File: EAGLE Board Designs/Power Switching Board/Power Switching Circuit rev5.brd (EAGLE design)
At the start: 100.3 x 86.1 mm, 69 parts, among them J1 CONNECTOR-4_SOURIAU_, J2 CONNECTOR-3_8STA20435PN, J3 CONNECTOR-4_SOURIAU_, K1 RELAY_SOLIDSTATE_NO_CMX60D20, Q1 TRANSISTOR_N_MOS_2-7K1S_TK100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, Q2 TRANSISTOR_N_MOS_2-7K1S_TK100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, Q3 TRANSISTOR_N_MOS_2-7K1S_TK100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, Q4 TRANSISTOR_N_MOS_2-7K1S_TK100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, U1 LTC4421

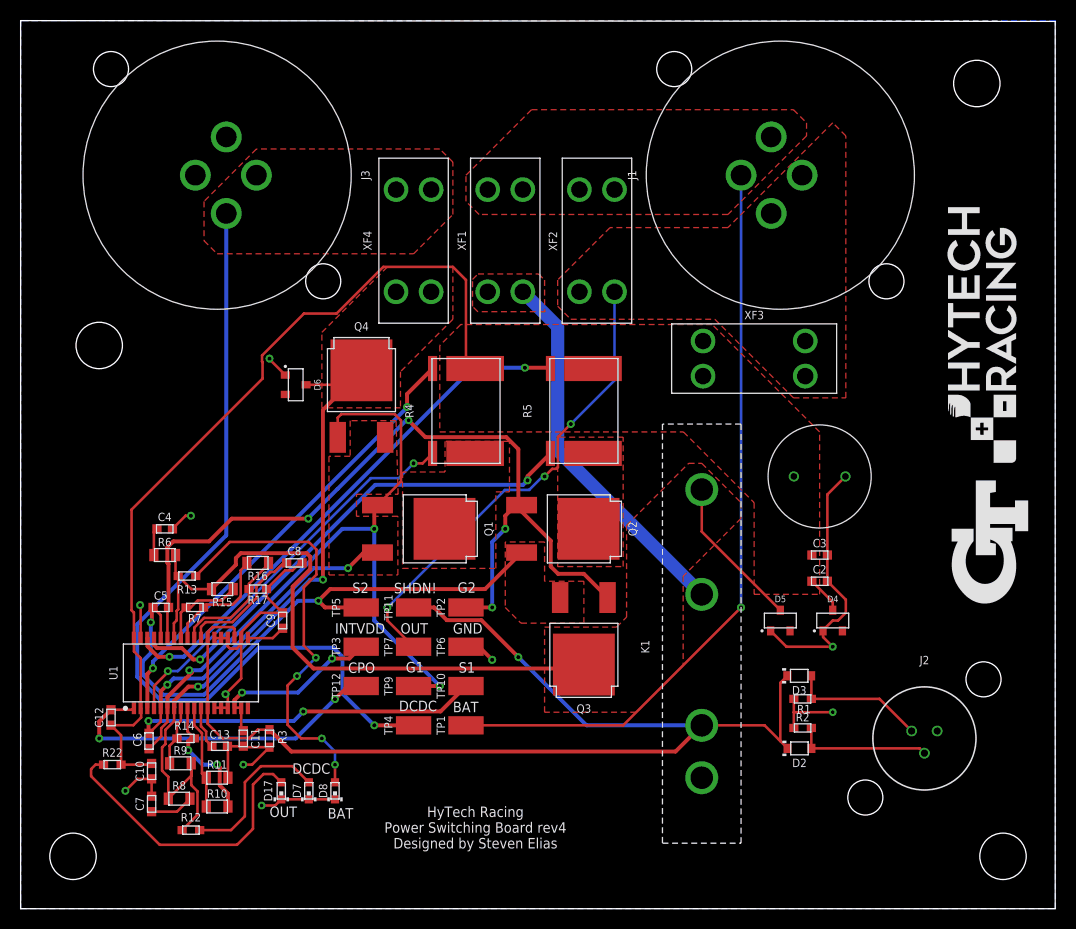
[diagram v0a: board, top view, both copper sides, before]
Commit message: Fixed issues with order of inputs to SSR
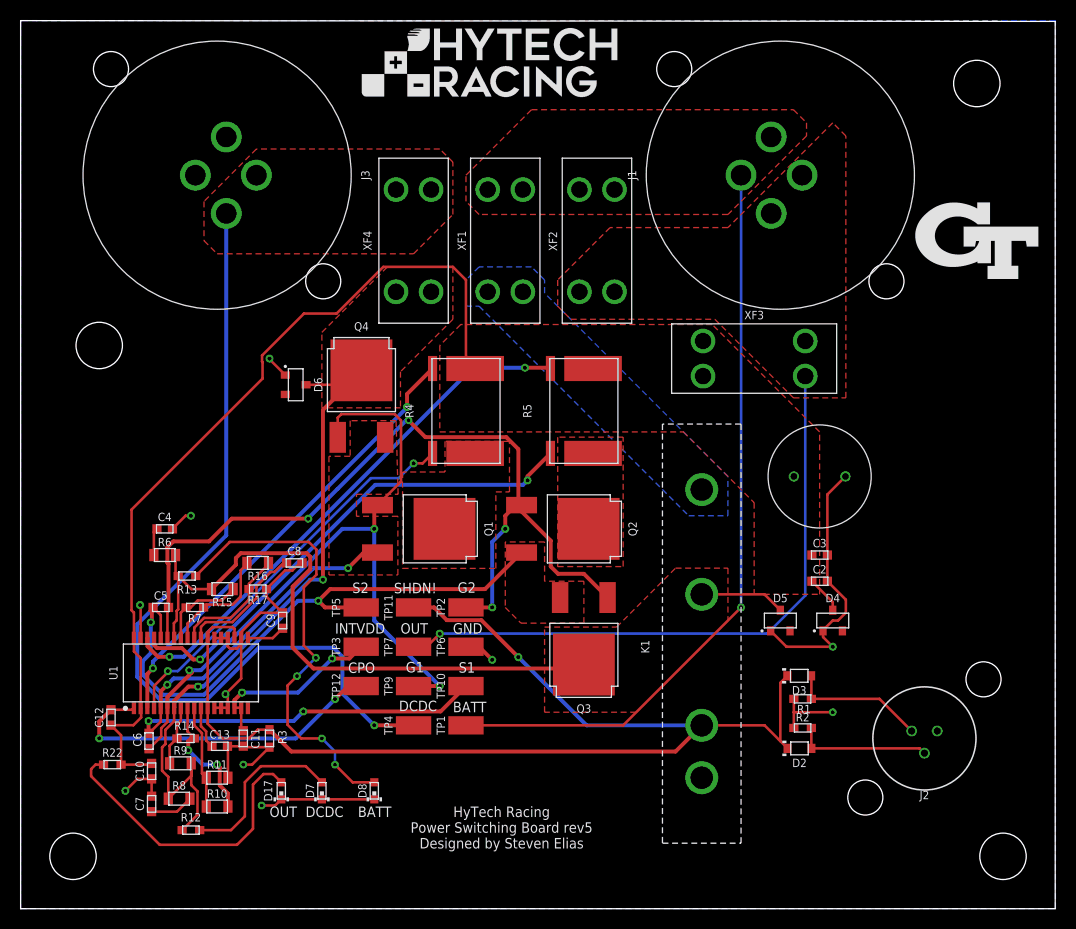
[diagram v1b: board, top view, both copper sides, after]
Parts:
- moved U$2 72.8 mm to (33.0, 78.7), turned to 0 degrees
- moved U$1 29.2 mm to (92.7, 64.8), turned to 0 degrees
- moved D8 3.81 mm to (34.3, 11.4)
- moved D7 1.27 mm to (29.2, 11.4)
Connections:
- removed net N$12: K1.2, XF1.1, XF1.2
- new net N$8: K1.1, XF1.1, XF1.2
- net BATTIN: now also K1.2; no longer K1.1
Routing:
- net N$12: track 36.5 -> 0.00 mm
- net OUT: track 46.3 -> 61.3 mm, vias 3 -> 1
- net BATTIN: track 77.3 -> 70.7 mm
- net GND: track 92.0 -> 95.8 mm
- net N$6: track 41.2 -> 44.0 mm
- net N$7: track 15.7 -> 17.0 mm
- net OUTPREFUSE: track 89.4 -> 88.2 mm
- added copper zone on layer 16, net N$8
- removed copper zone on layer 1, net N$12
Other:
- board text added: "BATT"
- board text added: "DO NOT INSTALL XF2 UNLESS BYPASSING ENTIRE CIRCUIT!"
- board text added: "HyTech Racing Power Switching Board rev5 Designed by Steven Elias"
- board text removed: "BAT"
- board text removed: "DO NOT INTALL XF2 UNLESS BYPASSING ENTIRE CIRCUIT!"
- board text removed: "HyTech Racing Power Switching Board rev4 Designed by Steven Elias"
